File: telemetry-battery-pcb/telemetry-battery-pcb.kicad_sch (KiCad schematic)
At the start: 71 parts, among them J1 Network Connector, J3 CONN_360410_MZC, J4 DS18B20, J5 CONN_360410_MZC, Q1 NMOS, Q2 PMOS, Q4 NMOS, U4 LTC2944, U5 XR76208, U6 M24C02-WMN, U8 DS2484R

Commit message: telemetry-battery-pcb: change value of resistance - R27 - C29 - C27/C28 and others
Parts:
- C24, C28: footprint Capacitor_SMD:C_0201_0603Metric -> Capacitor_SMD:C_1206_3216Metric; JLCPCB C1622 -> C96123
- C29: footprint Capacitor_SMD:C_0402_1005Metric -> Capacitor_SMD:C_0603_1608Metric; JLCPCB C1537 -> C1620
- R13: footprint Resistor_SMD:R_0201_0603Metric -> Resistor_SMD:R_0805_2012Metric; JLCPCB C22809 -> C17475
- R27: footprint Resistor_SMD:R_0402_1005Metric -> Resistor_SMD:R_0603_1608Metric; JLCPCB C25086 -> C22936
- RLIM1: footprint Resistor_SMD:R_0201_0603Metric -> Resistor_SMD:R_0402_1005Metric; JLCPCB C22843 -> C25867
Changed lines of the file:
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@@
 			)
 		)
-		(property "Footprint" "Resistor_SMD:R_0201_0603Metric"
+		(property "Footprint" "Resistor_SMD:R_0402_1005Metric"
 			(at 102.87 126.492 90)
 			(effects
@@
 			)
 		)
-		(property "JLCPCB" "C22843"
+		(property "JLCPCB" "C25867"
 			(at 102.87 128.27 90)
 			(effects
@@
 			)
 		)
-		(property "Footprint" "Capacitor_SMD:C_0201_0603Metric"
+		(property "Footprint" "Capacitor_SMD:C_1206_3216Metric"
 			(at 153.3652 137.16 0)
 			(effects
@@
 			)
 		)
-		(property "JLCPCB" "C1622"
+		(property "JLCPCB" "C96123"
 			(at 152.4 133.35 0)
 			(effects
@@
 			)
 		)
-		(property "Footprint" "Capacitor_SMD:C_0201_0603Metric"
+		(property "Footprint" "Capacitor_SMD:C_1206_3216Metric"
 			(at 143.2052 137.16 0)
 			(effects
@@
 			)
 		)
-		(property "JLCPCB" "C1622"
+		(property "JLCPCB" "C96123"
 			(at 142.24 133.35 0)
 			(effects
@@
 			)
 		)
-		(property "Footprint" "Resistor_SMD:R_0201_0603Metric"
+		(property "Footprint" "Resistor_SMD:R_0805_2012Metric"
 			(at 127.762 123.19 90)
 			(effects
@@
 			)
 		)
-		(property "JLCPCB" "C22809"
+		(property "JLCPCB" "C17475"
 			(at 129.54 123.19 0)
 			(effects
@@
 			)
 		)
-		(property "Footprint" "Capacitor_SMD:C_0402_1005Metric"
+		(property "Footprint" "Capacitor_SMD:C_0603_1608Metric"
 			(at 110.49 143.8148 0)
 			(effects
@@
 			)
 		)
-		(property "JLCPCB" "C1537"
+		(property "JLCPCB" "C1620"
 			(at 106.68 144.78 90)
 			(effects
@@
 			)
 		)
-		(property "Footprint" "Resistor_SMD:R_0402_1005Metric"
+		(property "Footprint" "Resistor_SMD:R_0603_1608Metric"
 			(at 116.84 138.938 90)
 			(effects
@@
 			)
 		)
-		(property "JLCPCB" "C25086"
+		(property "JLCPCB" "C22936"
 			(at 116.84 137.16 90)
 			(effects

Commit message: telemetry-battery-pcb: increase vias to 0.3mm  of the tps1htc30-q1
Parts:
- U7: footprint Package_SO:Texas_HTSSOP-14-1EP_4.4x5mm_P0.65mm_EP3.4x5mm_Mask3.155x3.255mm_ThermalVias -> Exocet:Tps1htc_Exocet_Texas_HTSSOP-14-1EP_4.4x5mm_P0.65mm_EP3.4x5mm_Mask3.155x3.255mm_ThermalVias
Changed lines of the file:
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@@
 			)
 		)
-		(property "Footprint" "Package_SO:Texas_HTSSOP-14-1EP_4.4x5mm_P0.65mm_EP3.4x5mm_Mask3.155x3.255mm_ThermalVias"
+		(property "Footprint" "Exocet:Tps1htc_Exocet_Texas_HTSSOP-14-1EP_4.4x5mm_P0.65mm_EP3.4x5mm_Mask3.155x3.255mm_ThermalVias"
 			(at 139.7 53.34 0)
 			(effects

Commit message: telemetry-battery-pcb: Review of pcb components and values
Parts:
- R12: JLCPCB C601838 -> C17797
- U7: value ~ -> Tps1htc
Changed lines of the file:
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@@
 			)
 		)
-		(property "JLCPCB" "C601838"
+		(property "JLCPCB" "C17797"
 			(at 135.89 123.19 0)
 			(effects
@@
 			)
 		)
-		(property "Value" "~"
+		(property "Value" "Tps1htc"
 			(at 139.7 53.34 0)
 			(effects

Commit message: telemetry-battery-pcb : Update PCB
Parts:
- R13: footprint Resistor_SMD:R_0805_2012Metric -> Resistor_SMD:R_0603_1608Metric; JLCPCB C17475 -> C22809
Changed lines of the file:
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@@
 			)
 		)
-		(property "Footprint" "Resistor_SMD:R_0805_2012Metric"
+		(property "Footprint" "Resistor_SMD:R_0603_1608Metric"
 			(at 127.762 123.19 90)
 			(effects
@@
 			)
 		)
-		(property "JLCPCB" "C17475"
+		(property "JLCPCB" "C22809"
 			(at 129.54 123.19 0)
 			(effects

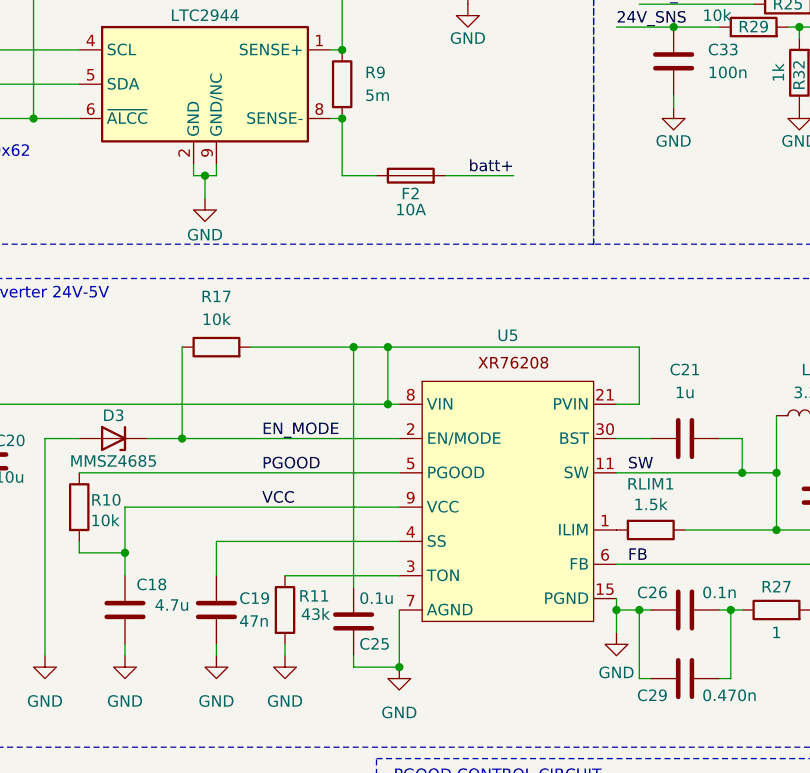
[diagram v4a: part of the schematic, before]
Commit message: telemetry-battery-pcb: components numbers JLCPCB and footprints change
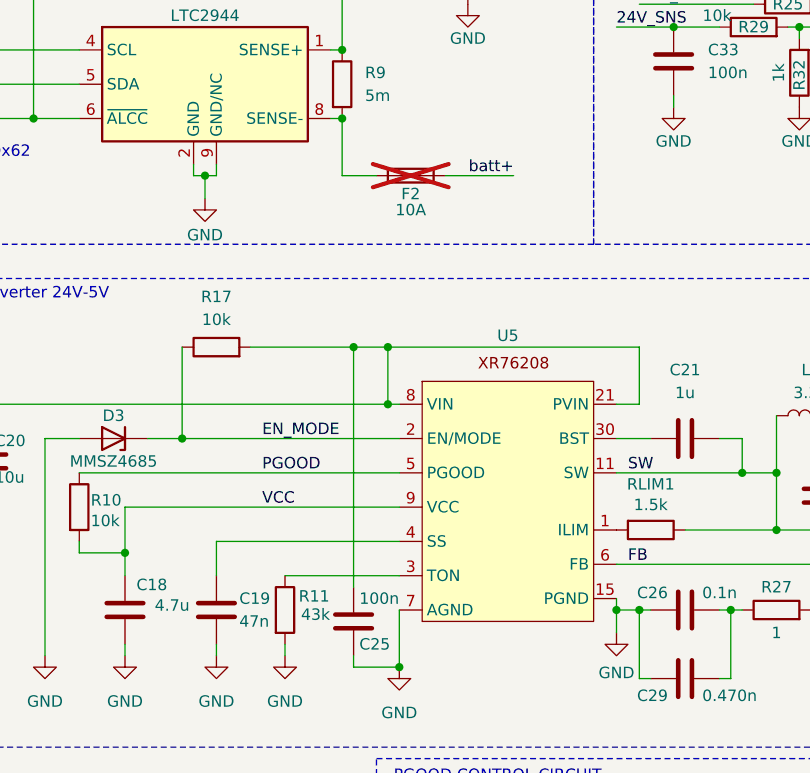
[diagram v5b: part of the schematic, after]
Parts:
- C19: footprint Capacitor_SMD:C_0402_1005Metric -> Capacitor_SMD:C_0201_0603Metric; JLCPCB C5142571 -> C1622
- C25: value 0.1u -> 100n
- C30: JLCPCB C1523 -> C1523
- D4: JLCPCB C2286 -> C2286
- F2: now not fitted
- R11: footprint Resistor_SMD:R_0402_1005Metric -> Resistor_SMD:R_0201_0603Metric; JLCPCB C8329 -> C23172
- R22: footprint Resistor_SMD:R_0805_2012Metric -> Resistor_SMD:R_0402_1005Metric; JLCPCB C17667 -> C4109
- RLIM1: footprint Resistor_SMD:R_0402_1005Metric -> Resistor_THT:R_Axial_DIN0207_L6.3mm_D2.5mm_P2.54mm_Vertical; JLCPCB C25867 -> C1370569
- U5: JLCPCB C555356 -> C1355299
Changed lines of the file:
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@@
 		)
 		(instances
-			(project ""
+			(project "telemetry-battery-pcb"
 				(path "/4b4cf3aa-c94c-4150-b9c5-35049cd71136"
 					(reference "Q1")
@@
 		)
 		(instances
-			(project ""
+			(project "telemetry-battery-pcb"
 				(path "/4b4cf3aa-c94c-4150-b9c5-35049cd71136"
 					(reference "#PWR043")
@@
 		)
 		(instances
-			(project ""
+			(project "telemetry-battery-pcb"
 				(path "/4b4cf3aa-c94c-4150-b9c5-35049cd71136"
 					(reference "L1")
@@
 		)
 		(instances
-			(project ""
+			(project "telemetry-battery-pcb"
 				(path "/4b4cf3aa-c94c-4150-b9c5-35049cd71136"
 					(reference "C26")
@@
 			)
 		)
-		(property "JLCPCB" "C555356"
+		(property "JLCPCB" "C1355299"
 			(at 87.63 105.41 0)
 			(effects
@@
 		)
 		(instances
-			(project ""
+			(project "telemetry-battery-pcb"
 				(path "/4b4cf3aa-c94c-4150-b9c5-35049cd71136"
 					(reference "U5")
@@
 		)
 		(instances
-			(project ""
+			(project "telemetry-battery-pcb"
 				(path "/4b4cf3aa-c94c-4150-b9c5-35049cd71136"
 					(reference "U6")
@@
 		)
 		(instances
-			(project ""
+			(project "telemetry-battery-pcb"
 				(path "/4b4cf3aa-c94c-4150-b9c5-35049cd71136"
 					(reference "#PWR037")
@@
 			)
 		)
-		(property "Footprint" "Resistor_SMD:R_0402_1005Metric"
+		(property "Footprint" "Resistor_SMD:R_0201_0603Metric"
 			(at 60.452 137.16 90)
 			(effects
@@
 			)
 		)
-		(property "JLCPCB" "C8329"
+		(property "JLCPCB" "C23172 "
 			(at 62.23 137.16 0)
 			(effects
@@
 		)
 		(instances
-			(project ""
+			(project "telemetry-battery-pcb"
 				(path "/4b4cf3aa-c94c-4150-b9c5-35049cd71136"
 					(reference "C22")
@@
 		)
 		(instances
-			(project ""
+			(project "telemetry-battery-pcb"
 				(path "/4b4cf3aa-c94c-4150-b9c5-35049cd71136"
 					(reference "D6")
@@
 			)
 		)
-		(property "Footprint" "Resistor_SMD:R_0402_1005Metric"
+		(property "Footprint" "Resistor_THT:R_Axial_DIN0207_L6.3mm_D2.5mm_P2.54mm_Vertical"
 			(at 102.87 126.492 90)
 			(effects
@@
 			)
 		)
-		(property "JLCPCB" "C25867"
+		(property "JLCPCB" "C1370569"
 			(at 102.87 128.27 90)
 			(effects
@@
 		)
 		(instances
-			(project ""
+			(project "telemetry-battery-pcb"
 				(path "/4b4cf3aa-c94c-4150-b9c5-35049cd71136"
 					(reference "R23")
@@
 		)
 		(instances
-			(project ""
+			(project "telemetry-battery-pcb"
 				(path "/4b4cf3aa-c94c-4150-b9c5-35049cd71136"
 					(reference "Q2")
@@
 		)
 		(instances
-			(project ""
+			(project "telemetry-battery-pcb"
 				(path "/4b4cf3aa-c94c-4150-b9c5-35049cd71136"
 					(reference "D3")
@@
 		)
 		(instances
-			(project ""
+			(project "telemetry-battery-pcb"
 				(path "/4b4cf3aa-c94c-4150-b9c5-35049cd71136"
 					(reference "#PWR035")
@@
 		)
 		(instances
-			(project ""
+			(project "telemetry-battery-pcb"
 				(path "/4b4cf3aa-c94c-4150-b9c5-35049cd71136"
 					(reference "U4")
@@
 		)
 		(instances
-			(project ""
+			(project "telemetry-battery-pcb"
 				(path "/4b4cf3aa-c94c-4150-b9c5-35049cd71136"
 					(reference "#PWR041")
@@
 		)
 		(instances
-			(project ""
+			(project "telemetry-battery-pcb"
 				(path "/4b4cf3aa-c94c-4150-b9c5-35049cd71136"
 					(reference "#PWR057")
@@
 			)
 		)
-		(property "Footprint" "Capacitor_SMD:C_0402_1005Metric"
+		(property "Footprint" "Capacitor_SMD:C_0201_0603Metric"
 			(at 55.5752 140.97 0)
 			(effects
@@
 			)
 		)
-		(property "JLCPCB" "C5142571"
+		(property "JLCPCB" "C1622 "
 			(at 54.61 137.16 0)
 			(effects
@@
 		)
 		(instances
-			(project ""
+			(project "telemetry-battery-pcb"
 				(path "/4b4cf3aa-c94c-4150-b9c5-35049cd71136"
 					(reference "C19")
@@
 		)
 		(instances
-			(project ""
+			(project "telemetry-battery-pcb"
 				(path "/4b4cf3aa-c94c-4150-b9c5-35049cd71136"
 					(reference "#PWR056")
@@
 		(in_bom yes)
 		(on_board yes)
-		(dnp no)
+		(dnp yes)
 		(property "Reference" "F2"
 			(at 76.2 90.932 90)
@@
 		)
 		(instances
-			(project ""
+			(project "telemetry-battery-pcb"
 				(path "/4b4cf3aa-c94c-4150-b9c5-35049cd71136"
 					(reference "J4")
@@
 		)
 		(instances
-			(project ""
+			(project "telemetry-battery-pcb"
 				(path "/4b4cf3aa-c94c-4150-b9c5-35049cd71136"
 					(reference "U7")
@@
 			)
 		)
-		(property "JLCPCB" " C2286"
+		(property "JLCPCB" "C2286"
 			(at 111.76 172.72 0)
 			(effects
@@
 		)
 		(instances
-			(project ""
+			(project "telemetry-battery-pcb"
 				(path "/4b4cf3aa-c94c-4150-b9c5-35049cd71136"
 					(reference "D4")
@@
 		)
 		(instances
-			(project ""
+			(project "telemetry-battery-pcb"
 				(path "/4b4cf3aa-c94c-4150-b9c5-35049cd71136"
 					(reference "R18")
@@
 		)
 		(instances
-			(project ""
+			(project "telemetry-battery-pcb"
 				(path "/4b4cf3aa-c94c-4150-b9c5-35049cd71136"
 					(reference "R10")
@@
 		)
 		(instances
-			(project ""
+			(project "telemetry-battery-pcb"
 				(path "/4b4cf3aa-c94c-4150-b9c5-35049cd71136"
 					(reference "#PWR067")
@@
 			)
 		)
-		(property "JLCPCB" " C1523"
+		(property "JLCPCB" "C1523"
 			(at 102.87 176.53 0)
 			(effects
@@
 		)
 		(instances
-			(project ""
+			(project "telemetry-battery-pcb"
 				(path "/4b4cf3aa-c94c-4150-b9c5-35049cd71136"
 					(reference "C30")
@@
 		)
 		(instances
-			(project ""
+			(project "telemetry-battery-pcb"
 				(path "/4b4cf3aa-c94c-4150-b9c5-35049cd71136"
 					(reference "R33")
@@
 		)
 		(instances
-			(project ""
+			(project "telemetry-battery-pcb"
 				(path "/4b4cf3aa-c94c-4150-b9c5-35049cd71136"
 					(reference "Q4")
@@
 		)
 		(instances
-			(project ""
+			(project "telemetry-battery-pcb"
 				(path "/4b4cf3aa-c94c-4150-b9c5-35049cd71136"
 					(reference "R14")
@@
 		)
 		(instances
-			(project ""
+			(project "telemetry-battery-pcb"
 				(path "/4b4cf3aa-c94c-4150-b9c5-35049cd71136"
 					(reference "#PWR038")
@@
 		)
 		(instances
-			(project ""
+			(project "telemetry-battery-pcb"
 				(path "/4b4cf3aa-c94c-4150-b9c5-35049cd71136"
 					(reference "C31")
@@
 			)
 		)
-		(property "Value" "0.1u"
+		(property "Value" "100n"
 			(at 70.485 135.89 0)
 			(effects
@@
 		)
 		(instances
-			(project ""
+			(project "telemetry-battery-pcb"
 				(path "/4b4cf3aa-c94c-4150-b9c5-35049cd71136"
 					(reference "C25")
@@
 		)
 		(instances
-			(project ""
+			(project "telemetry-battery-pcb"
 				(path "/4b4cf3aa-c94c-4150-b9c5-35049cd71136"
 					(reference "C18")
@@
 			)
 		)
-		(property "Footprint" "Resistor_SMD:R_0805_2012Metric"
+		(property "Footprint" "Resistor_SMD:R_0402_1005Metric"
 			(at 130.302 137.16 90)
 			(effects
@@
 			)
 		)
-		(property "JLCPCB" "C17667"
+		(property "JLCPCB" "C4109"
 			(at 132.08 137.16 0)
 			(effects
@@
 		)
 		(instances
-			(project ""
+			(project "telemetry-battery-pcb"
 				(path "/4b4cf3aa-c94c-4150-b9c5-35049cd71136"
 					(reference "J5")
@@
 		)
 		(instances
-			(project ""
+			(project "telemetry-battery-pcb"
 				(path "/4b4cf3aa-c94c-4150-b9c5-35049cd71136"
 					(reference "#PWR036")
@@
 		)
 		(instances
-			(project ""
+			(project "telemetry-battery-pcb"
 				(path "/4b4cf3aa-c94c-4150-b9c5-35049cd71136"
 					(reference "R27")
@@
 		)
 		(instances
-			(project ""
+			(project "telemetry-battery-pcb"
 				(path "/4b4cf3aa-c94c-4150-b9c5-35049cd71136"
 					(reference "#FLG01")
@@
 		)
 		(instances
-			(project ""
+			(project "telemetry-battery-pcb"
 				(path "/4b4cf3aa-c94c-4150-b9c5-35049cd71136"
 					(reference "R9")
@@
 		)
 		(instances
-			(project ""
+			(project "telemetry-battery-pcb"
 				(path "/4b4cf3aa-c94c-4150-b9c5-35049cd71136"
 					(reference "U8")

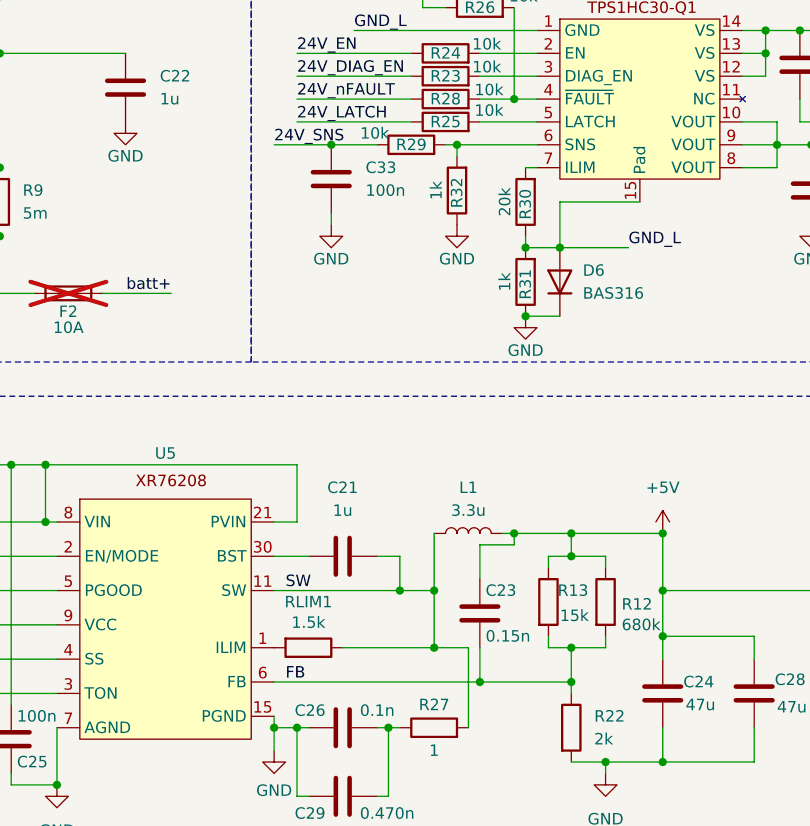
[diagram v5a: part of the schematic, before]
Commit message: telemetry-battery-pcb: Changes on footprints Rlim and R30
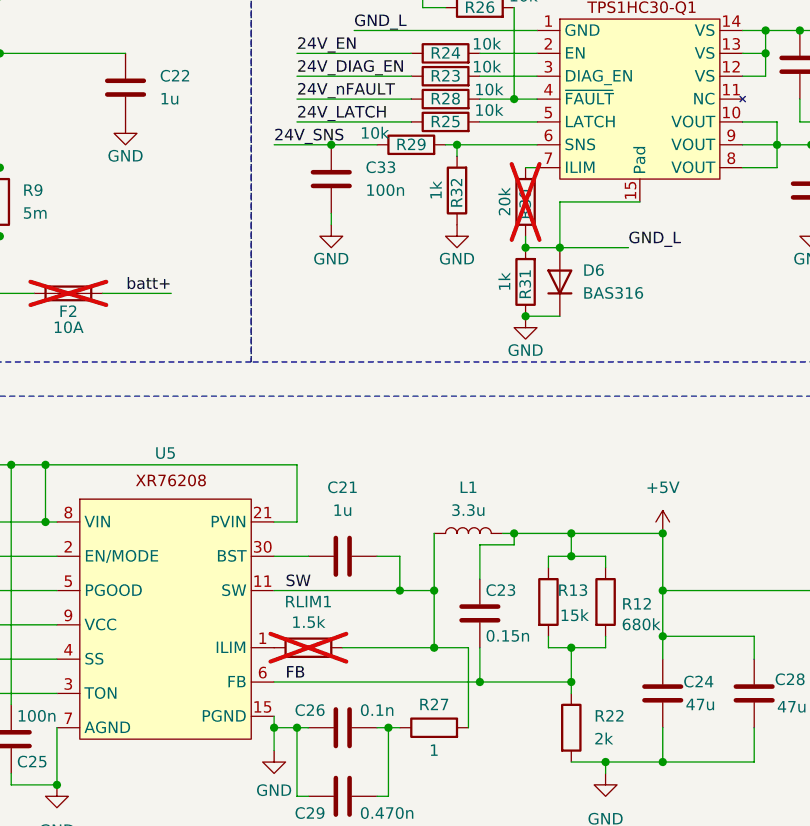
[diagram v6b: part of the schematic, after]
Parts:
- R30: footprint Resistor_SMD:R_0201_0603Metric -> Resistor_THT:R_Axial_DIN0309_L9.0mm_D3.2mm_P12.70mm_Horizontal; JLCPCB C4184 -> (none); now not fitted
- RLIM1: footprint Resistor_THT:R_Axial_DIN0207_L6.3mm_D2.5mm_P2.54mm_Vertical -> Resistor_THT:R_Axial_DIN0309_L9.0mm_D3.2mm_P12.70mm_Horizontal; JLCPCB C1370569 -> (none); now not fitted
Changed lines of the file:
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@@
 		(in_bom yes)
 		(on_board yes)
-		(dnp no)
+		(dnp yes)
 		(property "Reference" "R30"
 			(at 127 78.994 90)
@@
 			)
 		)
-		(property "Footprint" "Resistor_SMD:R_0201_0603Metric"
+		(property "Footprint" "Resistor_THT:R_Axial_DIN0309_L9.0mm_D3.2mm_P12.70mm_Horizontal"
 			(at 128.778 78.74 90)
 			(effects
@@
 		(property "Description" "Resistor"
 			(at 127 78.74 0)
-			(effects
-				(font
-					(size 1.27 1.27)
-				)
-				(hide yes)
-			)
-		)
-		(property "JLCPCB" "C4184"
-			(at 127 78.74 90)
 			(effects
 				(font
@@
 		(in_bom yes)
 		(on_board yes)
-		(dnp no)
+		(dnp yes)
 		(property "Reference" "RLIM1"
 			(at 102.87 123.19 90)
@@
 			)
 		)
-		(property "Footprint" "Resistor_THT:R_Axial_DIN0207_L6.3mm_D2.5mm_P2.54mm_Vertical"
+		(property "Footprint" "Resistor_THT:R_Axial_DIN0309_L9.0mm_D3.2mm_P12.70mm_Horizontal"
 			(at 102.87 126.492 90)
 			(effects
@@
 			(effects
 				(font
-					(size 1.27 1.27)
-				)
-				(hide yes)
-			)
-		)
-		(property "JLCPCB" "C1370569"
-			(at 102.87 128.27 90)
-			(effects
-				(font
